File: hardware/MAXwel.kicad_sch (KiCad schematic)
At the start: 155 parts, among them J1 Conn_02x05_Odd_Even, J2 Conn_02x12_Counter_Clockwise, J3 Barrel_Jack_Switch_Pin3Ring, SW1 SW_Push_Dual, SW10 SW_Wuerth_450301014042, SW11 SW_Wuerth_450301014042, SW12 SW_Wuerth_450301014042, SW13 SW_Wuerth_450301014042, SW2 SW_Push_Dual, SW3 SW_Push_Dual, SW4 SW_Push_Dual, SW5 SW_Wuerth_450301014042, SW6 SW_Wuerth_450301014042, SW7 SW_Wuerth_450301014042, SW8 SW_Wuerth_450301014042, SW9 SW_Push_DPDT, U1 D168K, U2 D168K, U3 D168K, U4 D168K, U5 EPM240T100, U6 AMS1117-3.3, X1 50.000, X2 14.756

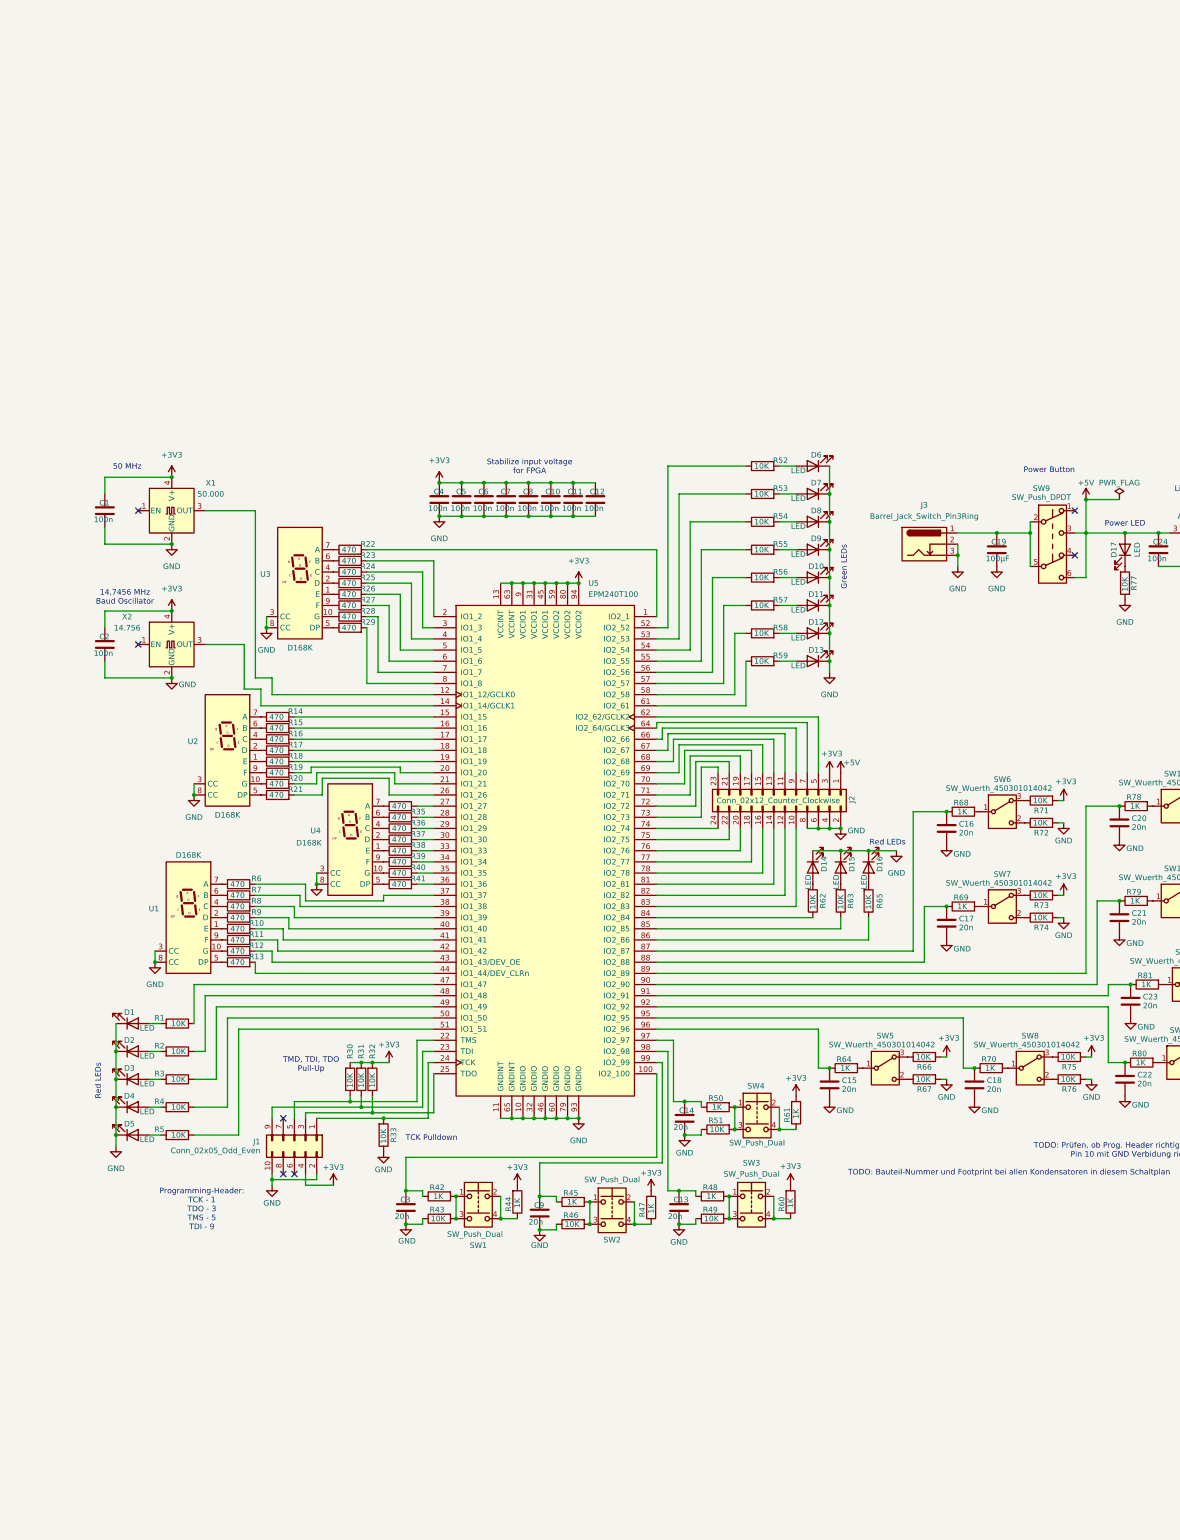
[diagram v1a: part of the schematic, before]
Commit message: change resistor and capacitor size, rearrange pinheader and 7-seg connections
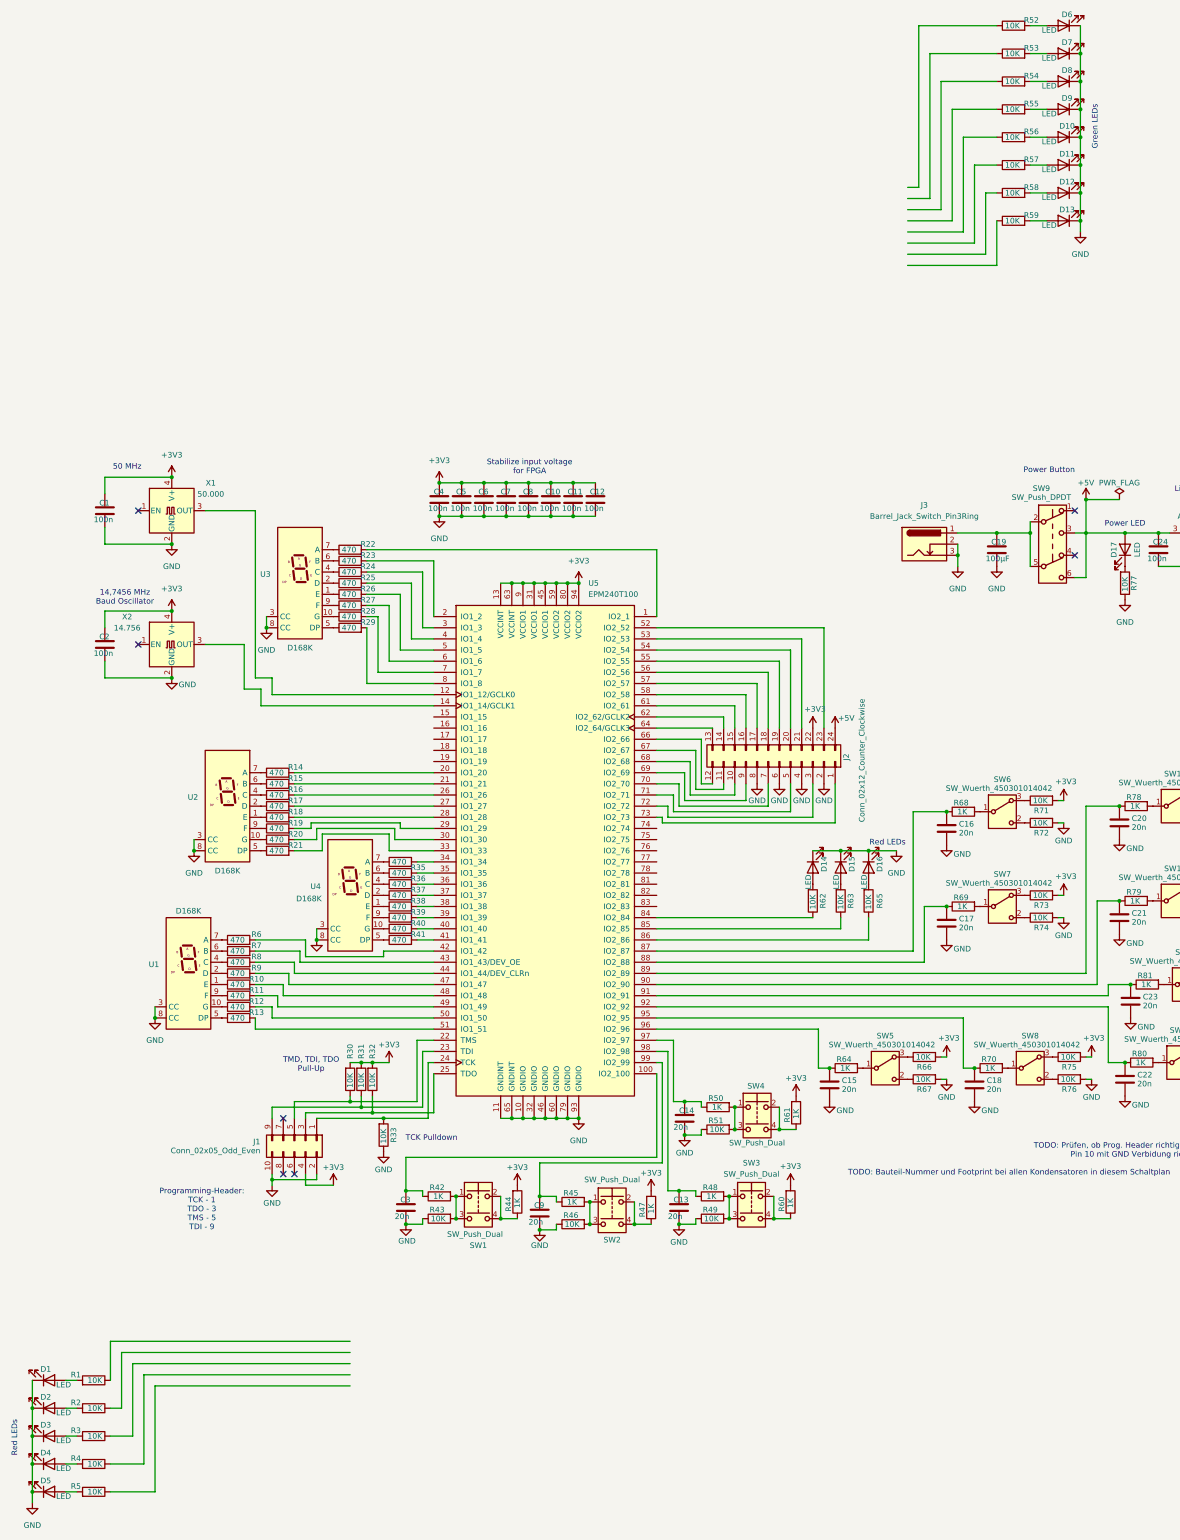
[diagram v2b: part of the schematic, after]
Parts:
- C1, C10, C11, C12, C13, C14, C15, C16, C17, C18, C2, C20, C21, C22, C23, C24, C25, C3, C4, C5, C6, C7, C8, C9: footprint Capacitor_SMD:C_0805_2012Metric_Pad1.18x1.45mm_HandSolder -> Capacitor_SMD:C_0603_1608Metric_Pad1.08x0.95mm_HandSolder
- J2: symbol Connector_Generic:Conn_02x12_Odd_Even -> Connector_Generic:Conn_02x12_Counter_Clockwise
- R1, R10, R11, R12, R13, R14, R15, R16, R17, R18, R19, R2, R20, R21, R22, R23, R24, R25, R26, R27, R28, R29, R3, R30, R31, R32, R33, R34, R35, R36, R37, R38, R39, R4, R40, R41, R42, R43, R44, R45, R46, R47, R48, R49, R5, R50, R51, R52, R53, R54, R55, R56, R57, R58, R59, R6, R60, R61, R62, R63, R64, R65, R66, R67, R68, R69, R7, R70, R71, R72, R73, R74, R75, R76, R77, R78, R79, R8, R80, R81, R82, R83, R84, R85, R86, R87, R88, R89, R9: footprint Resistor_SMD:R_0805_2012Metric_Pad1.20x1.40mm_HandSolder -> Resistor_SMD:R_0603_1608Metric_Pad0.98x0.95mm_HandSolder
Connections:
- net +3V3: now also J2.22 (Pin_22); no longer J2.3 (Pin_3)
- net +5V: now also J2.24 (Pin_24); no longer J2.1 (Pin_1)
- net at R18.2: now also U5.28 (IO1_28); no longer U5.19 (IO1_19)
- net at R59.1: no longer U5.61 (IO2_61)
- net at R17.2: now also U5.27 (IO1_27); no longer U5.18 (IO1_18)
- net at R35.2: now also U5.35 (IO1_35); no longer U5.28 (IO1_28)
- net at R1.1: no longer U5.47 (IO1_47)
- net at U5.15 (IO1_15): no longer R14.2
- net at U5.16 (IO1_16): no longer R15.2
- net at U5.17 (IO1_17): no longer R16.2
- net at U5.20 (IO1_20): now also R14.2; no longer R19.2
- net at U5.21 (IO1_21): now also R15.2; no longer R20.2
- net at U5.26 (IO1_26): now also R16.2; no longer R21.2
- net at R34.2: now also U5.34 (IO1_34); no longer U5.27 (IO1_27)
- net at U5.29 (IO1_29): now also R19.2; no longer R36.2
- net at U5.30 (IO1_30): now also R20.2; no longer R37.2
- net at U5.33 (IO1_33): now also R21.2; no longer R38.2
- net at R39.2: now also U5.39 (IO1_39); no longer U5.34 (IO1_34)
- net at R40.2: now also U5.40 (IO1_40); no longer U5.35 (IO1_35)
- net at U5.36 (IO1_36): now also R36.2; no longer R41.2
- net at U5.37 (IO1_37): now also R37.2; no longer R6.2
- net at U5.38 (IO1_38): now also R38.2; no longer R7.2
- net at R8.2: now also U5.44 (IO1_44/DEV_CLRn); no longer U5.39 (IO1_39)
- net at R9.2: now also U5.47 (IO1_47); no longer U5.40 (IO1_40)
- net at U5.41 (IO1_41): now also R41.2; no longer R10.2
- net at U5.42 (IO1_42): now also R6.2; no longer R11.2
- net at U5.43 (IO1_43/DEV_OE): now also R7.2; no longer R12.2
- net at R13.2: now also U5.51 (IO1_51); no longer U5.44 (IO1_44/DEV_CLRn)
- net at U5.48 (IO1_48): now also R10.2; no longer R2.1
- net at U5.49 (IO1_49): now also R11.2; no longer R3.1
- net at U5.50 (IO1_50): now also R12.2; no longer R4.1
- net at R5.1: no longer U5.51 (IO1_51)
- net at U5.52 (IO2_52): now also J2.23 (Pin_23); no longer R52.1
- net at U5.53 (IO2_53): now also J2.21 (Pin_21); no longer R53.1
- net at U5.54 (IO2_54): now also J2.20 (Pin_20); no longer R54.1
- net at U5.55 (IO2_55): now also J2.19 (Pin_19); no longer R55.1
- net at U5.56 (IO2_56): now also J2.18 (Pin_18); no longer R56.1
- net at U5.57 (IO2_57): now also J2.17 (Pin_17); no longer R57.1
- net at U5.58 (IO2_58): now also J2.16 (Pin_16); no longer R58.1
- net at U5.62 (IO2_62/GCLK2): now also J2.14 (Pin_14); no longer J2.5 (Pin_5)
- net at U5.64 (IO2_64/GCLK3): now also J2.13 (Pin_13); no longer J2.7 (Pin_7)
- net at U5.66 (IO2_66): now also J2.12 (Pin_12); no longer J2.9 (Pin_9)
- net at U5.68 (IO2_68): now also J2.10 (Pin_10); no longer J2.13 (Pin_13)
- net at J2.15 (Pin_15): now also U5.61 (IO2_61); no longer U5.69 (IO2_69)
- net at U5.70 (IO2_70): now also J2.7 (Pin_7); no longer J2.17 (Pin_17)
- net at U5.71 (IO2_71): now also J2.5 (Pin_5); no longer J2.19 (Pin_19)
- net at U5.72 (IO2_72): now also J2.3 (Pin_3); no longer J2.21 (Pin_21)
- net at U5.73 (IO2_73): now also J2.1 (Pin_1); no longer J2.23 (Pin_23)
- net at U5.74 (IO2_74): no longer J2.24 (Pin_24)
- net at U5.75 (IO2_75): no longer J2.22 (Pin_22)
- net at U5.76 (IO2_76): no longer J2.20 (Pin_20)
- net at U5.77 (IO2_77): no longer J2.18 (Pin_18)
- net at U5.78 (IO2_78): no longer J2.16 (Pin_16)
- net at U5.81 (IO2_81): no longer J2.14 (Pin_14)
- net at U5.82 (IO2_82): no longer J2.12 (Pin_12)
- net at U5.83 (IO2_83): no longer J2.10 (Pin_10)
- new net: J2.9 (Pin_9), U5.69 (IO2_69)
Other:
- moved on the sheet: D1, D10, D11, D12, D13, D2, D3, D4, D5, D6, D7, D8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

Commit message: rotation of FPGA
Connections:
- net at C15.1, R64.1: no longer U5.96 (IO2_96)
- net at R18.1: now also U2.9 (F); no longer U2.1 (E)
- net at R18.2: now also U5.40 (IO1_40); no longer U5.28 (IO1_28)
- net at C20.1, R78.1: no longer U5.89 (IO2_89)
- net at C17.1, R69.1: no longer U5.88 (IO2_88)
- net at R17.1: now also U2.7 (A); no longer U2.2 (D)
- net at R17.2: now also U5.39 (IO1_39); no longer U5.27 (IO1_27)
- net at C16.1, R68.1: no longer U5.87 (IO2_87)
- net at C3.1, R42.1: no longer U5.100 (IO2_100)
- net at R35.2: now also U5.47 (IO1_47); no longer U5.35 (IO1_35)
- net at C22.1, R80.1: no longer U5.92 (IO2_92)
- net at U1.1 (E): now also R13.1; no longer R10.1
- net at U1.2 (D): now also R11.1; no longer R9.1
- net at U1.5 (DP): now also R6.1; no longer R13.1
- net at U1.7 (A): now also R9.1; no longer R6.1
- net at U1.9 (F): now also R10.1; no longer R11.1
- net at U5.1 (IO2_1): no longer R22.2
- net at U5.2 (IO1_2): no longer R23.2
- net at U5.20 (IO1_20): no longer R14.2
- net at U5.21 (IO1_21): no longer R15.2
- net at U5.26 (IO1_26): now also R22.2; no longer R16.2
- net at U5.29 (IO1_29): now also R25.2; no longer R19.2
- net at R24.2: now also U5.28 (IO1_28); no longer U5.3 (IO1_3)
- net at U5.30 (IO1_30): now also R26.2; no longer R20.2
- net at U5.33 (IO1_33): now also R27.2; no longer R21.2
- net at U5.34 (IO1_34): now also R28.2; no longer R34.2
- net at U5.36 (IO1_36): now also R14.2; no longer R36.2
- net at U5.37 (IO1_37): now also R15.2; no longer R37.2
- net at U5.38 (IO1_38): now also R16.2; no longer R38.2
- net at R39.2: now also U5.51 (IO1_51); no longer U5.39 (IO1_39)
- net at U5.4 (IO1_4): no longer R25.2
- net Bridge_2: now reaches R40.2
- net Bridge_2: now also U5.53 (IO2_53); no longer U5.40 (IO1_40)
- net at U5.41 (IO1_41): now also R19.2; no longer R41.2
- net at U5.42 (IO1_42): now also R20.2; no longer R6.2
- net at U5.43 (IO1_43/DEV_OE): now also R21.2; no longer R7.2
- net at U5.44 (IO1_44/DEV_CLRn): now also R34.2; no longer R8.2
- net at R9.2: now also U5.57 (IO2_57); no longer U5.47 (IO1_47)
- net at U5.48 (IO1_48): now also R36.2; no longer R10.2
- net at U5.49 (IO1_49): now also R37.2; no longer R11.2
- net at U5.5 (IO1_5): no longer R26.2
- net at U5.50 (IO1_50): now also R38.2; no longer R12.2
- net at R13.2: now also U5.64 (IO2_64/GCLK3); no longer U5.51 (IO1_51)
- net at J2.23 (Pin_23): now also U5.66 (IO2_66); no longer U5.52 (IO2_52)
- net at J2.21 (Pin_21): now also U5.67 (IO2_67); no longer U5.53 (IO2_53)
- net at U5.54 (IO2_54): now also R6.2; no longer J2.20 (Pin_20)
- net at U5.55 (IO2_55): now also R7.2; no longer J2.19 (Pin_19)
- net at U5.56 (IO2_56): now also R8.2; no longer J2.18 (Pin_18)
- net at J2.17 (Pin_17): now also U5.71 (IO2_71); no longer U5.57 (IO2_57)
- net at U5.58 (IO2_58): now also R10.2; no longer J2.16 (Pin_16)
- net at U5.6 (IO1_6): no longer R27.2
- net at U5.61 (IO2_61): now also R11.2; no longer J2.15 (Pin_15)
- net at U5.62 (IO2_62/GCLK2): now also R12.2; no longer J2.14 (Pin_14)
- net at J2.13 (Pin_13): now also U5.75 (IO2_75); no longer U5.64 (IO2_64/GCLK3)
- net at J2.12 (Pin_12): now also U5.76 (IO2_76); no longer U5.66 (IO2_66)
- net at J2.11 (Pin_11): now also U5.77 (IO2_77); no longer U5.67 (IO2_67)
- net at U5.68 (IO2_68): now also J2.20 (Pin_20); no longer J2.10 (Pin_10)
- net at U5.69 (IO2_69): now also J2.19 (Pin_19); no longer J2.9 (Pin_9)
- net at U5.7 (IO1_7): no longer R28.2
- net at U5.70 (IO2_70): now also J2.18 (Pin_18); no longer J2.7 (Pin_7)
- net at J2.5 (Pin_5): now also U5.83 (IO2_83); no longer U5.71 (IO2_71)
- net at U5.72 (IO2_72): now also J2.16 (Pin_16); no longer J2.3 (Pin_3)
- net at U5.73 (IO2_73): now also J2.15 (Pin_15); no longer J2.1 (Pin_1)
- net at U5.74 (IO2_74): now also J2.14 (Pin_14)
- net at U5.78 (IO2_78): now also J2.10 (Pin_10)
- net at R29.2: now also U5.35 (IO1_35); no longer U5.8 (IO1_8)
- net at U5.81 (IO2_81): now also J2.9 (Pin_9)
- net at U5.82 (IO2_82): now also J2.7 (Pin_7)
- net at U5.84 (IO2_84): now also J2.3 (Pin_3); no longer R62.1
- net at U5.85 (IO2_85): now also J2.1 (Pin_1); no longer R63.1
- net at U5.86 (IO2_86): no longer R65.1
- net at C21.1, R79.1: no longer U5.90 (IO2_90)
- net at C23.1, R81.1: no longer U5.91 (IO2_91)
- net at C18.1, R70.1: no longer U5.95 (IO2_95)
- net at C14.1, R50.1: no longer U5.97 (IO2_97)
- net at C13.1, R48.1: no longer U5.98 (IO2_98)
- net at C9.1, R45.1: no longer U5.99 (IO2_99)
- net at R37.1: now also U4.7 (A); no longer U4.2 (D)
- net at R41.1: now also U4.1 (E); no longer U4.5 (DP)
- net at R19.1: now also U2.2 (D); no longer U2.9 (F)
- net at R38.1: now also U4.9 (F); no longer U4.1 (E)
- net at R39.1: now also U4.2 (D); no longer U4.9 (F)
- net at R34.1: now also U4.5 (DP); no longer U4.7 (A)
- net at R21.1: now also U2.1 (E); no longer U2.5 (DP)
- net at R26.1: now also U3.9 (F); no longer U3.1 (E)
- net at U3.2 (D): now also R27.1; no longer R25.1
- net at R29.1: now also U3.1 (E); no longer U3.5 (DP)
- net at R22.1: now also U3.5 (DP); no longer U3.7 (A)
- net at R14.1: now also U2.5 (DP); no longer U2.7 (A)
- new net: R23.2, U5.27 (IO1_27)
- new net: R25.1, U3.7 (A)
- new net Bridge_1: R41.2, U5.52 (IO2_52)
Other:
- moved on the sheet: C13, C14, C15, C16, C17, C18, C20, C21, C22, C23, C3, C9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

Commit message: arranged mostly all parts to reduce intersections
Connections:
- net Bridge_1: now also U5.53 (IO2_53); no longer U5.52 (IO2_52)
- net Bridge_2: now also U5.52 (IO2_52); no longer U5.53 (IO2_53)
- net at C15.1, R64.1: now also U5.2 (IO1_2)
- net at C20.1, R78.1: now also U5.90 (IO2_90)
- net at R59.1: now also U5.87 (IO2_87)
- net at C17.1, R69.1: now also U5.88 (IO2_88)
- net at C16.1, R68.1: now also U5.86 (IO2_86)
- net at C22.1, R80.1: now also U5.98 (IO2_98)
- net at U5.1 (IO2_1): now also R53.1
- net at U5.100 (IO2_100): now also C18.1, R70.1
- net at U5.3 (IO1_3): now also R52.1
- net at U5.89 (IO2_89): now also R58.1
- net at U5.91 (IO2_91): now also R57.1
- net at U5.92 (IO2_92): now also C21.1, R79.1
- net at U5.95 (IO2_95): now also R56.1
- net at U5.96 (IO2_96): now also C23.1, R81.1
- net at U5.97 (IO2_97): now also R55.1
- net at U5.99 (IO2_99): now also R54.1
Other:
- note added: "Green LED"
- note removed: "Green LEDs"
- moved on the sheet: C1, C10, C11, C12, C15, C16, C17, C18, C19, C2, C20, C21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
